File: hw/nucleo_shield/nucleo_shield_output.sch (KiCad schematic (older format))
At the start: 4 parts, among them P2 CONN_01X10, P3 CONN_01X10, U1 74HC595, U2 74HC595

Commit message: Update schematic to add sct and io expander
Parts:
- U1, U2: footprint Housings_DIP:DIP-16__300 -> Housings_DIP:DIP-16_W7.62mm
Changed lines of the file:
@@
 LIBS:memory
 LIBS:xilinx
-LIBS:special
 LIBS:microcontrollers
 LIBS:dsp
@@
 F 0 "U1" H 4650 3250 70  0000 C CNN
 F 1 "74HC595" H 4500 2050 70  0000 C CNN
-F 2 "Housings_DIP:DIP-16__300" H 4500 2650 60  0001 C CNN
+F 2 "Housings_DIP:DIP-16_W7.62mm" H 4500 2650 60  0001 C CNN
 F 3 "" H 4500 2650 60  0000 C CNN
 	1    4500 2650
@@
 $EndComp
 $Comp
-L GND #PWR012
+L GND #PWR021
 U 1 1 5729AB4A
 P 3800 3050
-F 0 "#PWR012" H 3800 2800 50  0001 C CNN
+F 0 "#PWR021" H 3800 2800 50  0001 C CNN
 F 1 "GND" H 3800 2900 50  0000 C CNN
 F 2 "" H 3800 3050 60  0000 C CNN
@@
 $EndComp
 $Comp
-L GND #PWR013
+L GND #PWR022
 U 1 1 5729AB50
 P 3800 4650
-F 0 "#PWR013" H 3800 4400 50  0001 C CNN
+F 0 "#PWR022" H 3800 4400 50  0001 C CNN
 F 1 "GND" H 3800 4500 50  0000 C CNN
 F 2 "" H 3800 4650 60  0000 C CNN
@@
 	7950 4400 8050 4400
 $Comp
-L GND #PWR014
+L GND #PWR023
 U 1 1 5729ABA1
 P 7000 2100
-F 0 "#PWR014" H 7000 1850 50  0001 C CNN
+F 0 "#PWR023" H 7000 1850 50  0001 C CNN
 F 1 "GND" H 7000 1950 50  0000 C CNN
 F 2 "" H 7000 2100 60  0000 C CNN
@@
 	7500 3700 8050 3700
 $Comp
-L +5V #PWR015
+L +5V #PWR024
 U 1 1 5729ABA8
 P 7000 2000
-F 0 "#PWR015" H 7000 1850 50  0001 C CNN
+F 0 "#PWR024" H 7000 1850 50  0001 C CNN
 F 1 "+5V" H 7000 2140 50  0000 C CNN
 F 2 "" H 7000 2000 60  0000 C CNN
@@
 $EndComp
 $Comp
-L +5V #PWR016
+L +5V #PWR025
 U 1 1 5729ABBE
 P 7100 4600
-F 0 "#PWR016" H 7100 4450 50  0001 C CNN
+F 0 "#PWR025" H 7100 4450 50  0001 C CNN
 F 1 "+5V" H 7100 4740 50  0000 C CNN
 F 2 "" H 7100 4600 60  0000 C CNN
@@
 $EndComp
 $Comp
-L GND #PWR017
+L GND #PWR026
 U 1 1 5729ABC4
 P 7100 4500
-F 0 "#PWR017" H 7100 4250 50  0001 C CNN
+F 0 "#PWR026" H 7100 4250 50  0001 C CNN
 F 1 "GND" H 7100 4350 50  0000 C CNN
 F 2 "" H 7100 4500 60  0000 C CNN
@@
 F 0 "U2" H 4650 4850 70  0000 C CNN
 F 1 "74HC595" H 4500 3650 70  0000 C CNN
-F 2 "Housings_DIP:DIP-16__300" H 4500 4250 60  0001 C CNN
+F 2 "Housings_DIP:DIP-16_W7.62mm" H 4500 4250 60  0001 C CNN
 F 3 "" H 4500 4250 60  0000 C CNN
 	1    4500 4250
@@
 $EndComp
 $Comp
-L +5V #PWR018
+L +5V #PWR027
 U 1 1 5729ABD5
 P 4200 1900
-F 0 "#PWR018" H 4200 1750 50  0001 C CNN
+F 0 "#PWR027" H 4200 1750 50  0001 C CNN
 F 1 "+5V" H 4200 2040 50  0000 C CNN
 F 2 "" H 4200 1900 60  0000 C CNN
@@
 $EndComp
 $Comp
-L +5V #PWR019
+L +5V #PWR028
 U 1 1 5729ABDB
 P 5900 3550
-F 0 "#PWR019" H 5900 3400 50  0001 C CNN
+F 0 "#PWR028" H 5900 3400 50  0001 C CNN
 F 1 "+5V" H 5900 3690 50  0000 C CNN
 F 2 "" H 5900 3550 60  0000 C CNN
@@
 	5200 3350 5200 3100
 $Comp
-L +5V #PWR020
+L +5V #PWR029
 U 1 1 5729ABE8
 P 2500 2500
-F 0 "#PWR020" H 2500 2350 50  0001 C CNN
+F 0 "#PWR029" H 2500 2350 50  0001 C CNN
 F 1 "+5V" H 2500 2640 50  0000 C CNN
 F 2 "" H 2500 2500 60  0000 C CNN
@@
 $EndComp
 $Comp
-L +5V #PWR021
+L +5V #PWR030
 U 1 1 5729ABEE
 P 3050 4100
-F 0 "#PWR021" H 3050 3950 50  0001 C CNN
+F 0 "#PWR030" H 3050 3950 50  0001 C CNN
 F 1 "+5V" H 3050 4240 50  0000 C CNN
 F 2 "" H 3050 4100 60  0000 C CNN

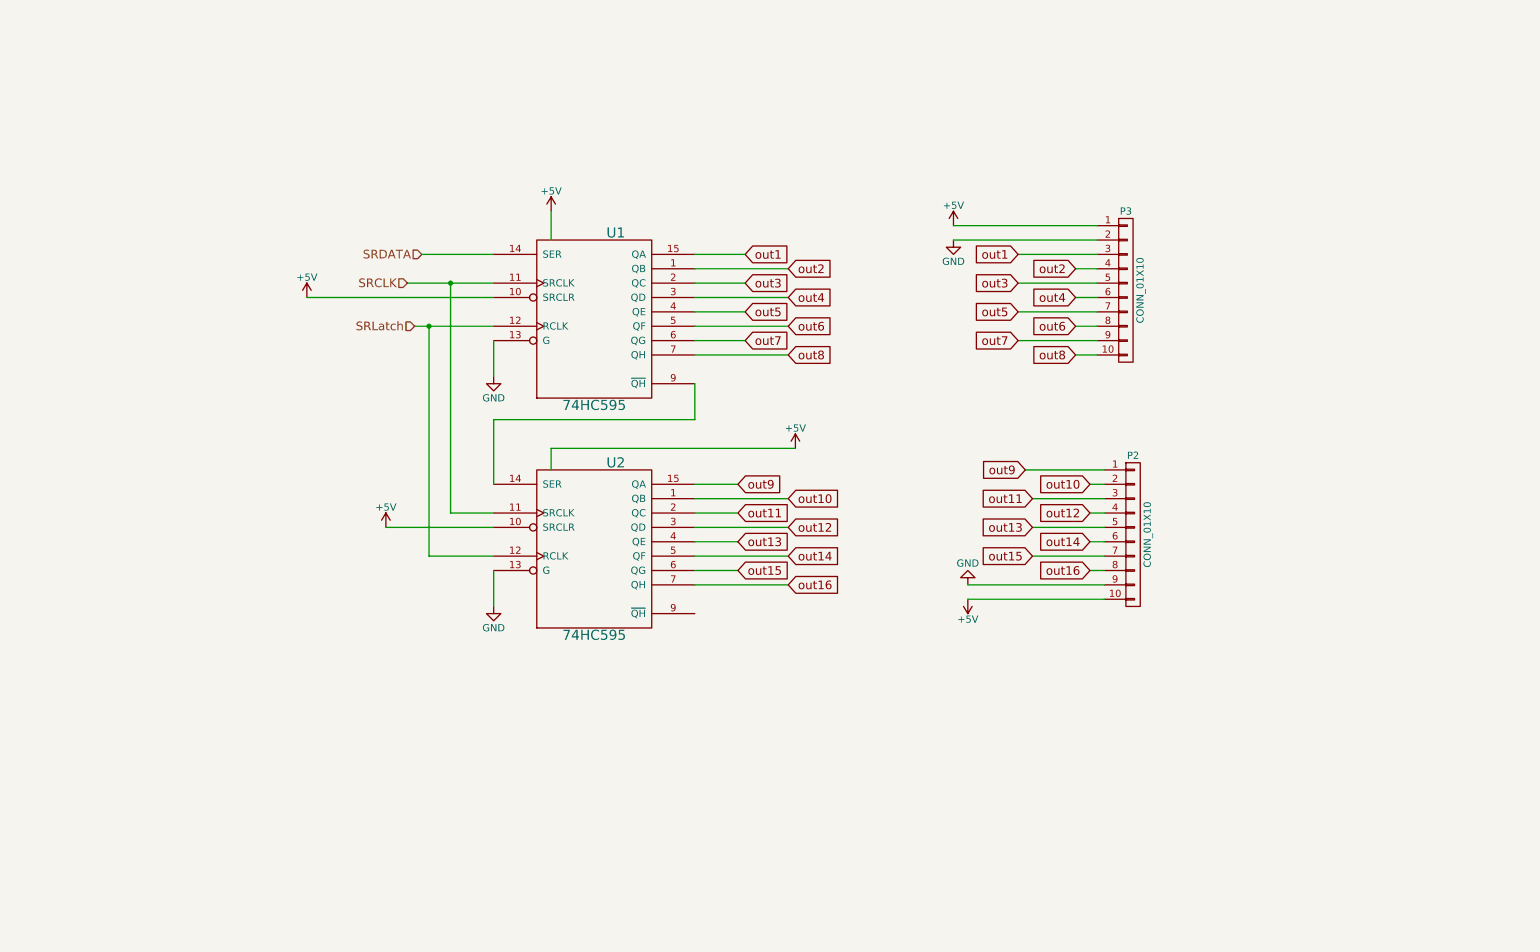
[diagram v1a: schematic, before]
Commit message: Hw: add intermediate header between output and ULN2803
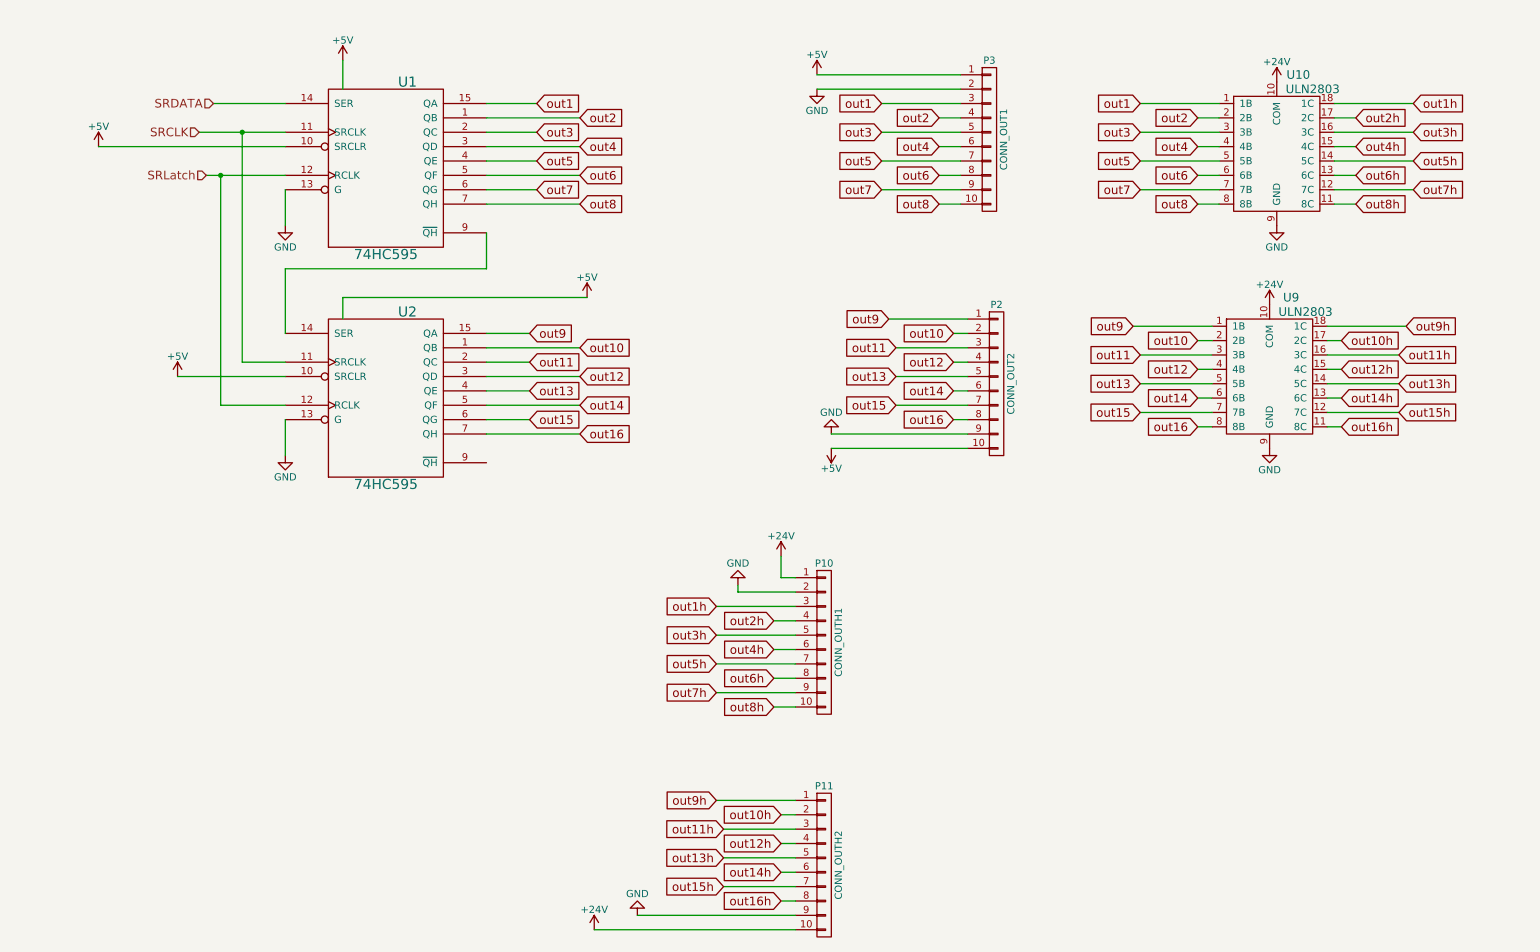
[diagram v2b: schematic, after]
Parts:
- added P10: CONN_OUTH1, w_conn_screw:mors_10p, symbol CONN_01X10
- added P11: CONN_OUTH2, w_conn_screw:mors_10p, symbol CONN_01X10
- added U10, U9: ULN2803, Housings_DIP:DIP-18__300, symbol ULN2803
- P2: value CONN_01X10 -> CONN_OUT2; footprint w_conn_screw:mors_10p -> Pin_Headers:Pin_Header_Straight_1x10
- P3: value CONN_01X10 -> CONN_OUT1; footprint w_conn_screw:mors_10p -> Pin_Headers:Pin_Header_Straight_1x10
- U1, U2: footprint Housings_DIP:DIP-16_W7.62mm -> Housings_DIP:DIP-16__300
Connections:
- net GND: now also P10.2 (P2), P11.9 (P9), U10.9 (GND), U9.9 (GND)
- net out1: now also U10.1 (1B)
- net out10: now also U9.2 (2B)
- net out11: now also U9.3 (3B)
- net out12: now also U9.4 (4B)
- net out13: now also U9.5 (5B)
- net out14: now also U9.6 (6B)
- net out15: now also U9.7 (7B)
- net out16: now also U9.8 (8B)
- net out2: now also U10.2 (2B)
- net out3: now also U10.3 (3B)
- net out4: now also U10.4 (4B)
- net out5: now also U10.5 (5B)
- net out6: now also U10.6 (6B)
- net out7: now also U10.7 (7B)
- net out8: now also U10.8 (8B)
- net out9: now also U9.1 (1B)
- new net +24V: P10.1 (P1), P11.10 (P10), U10.10 (COM), U9.10 (COM)
- new net out10h: P11.2 (P2), U9.17 (2C)
- new net out11h: P11.3 (P3), U9.16 (3C)
- new net out12h: P11.4 (P4), U9.15 (4C)
- new net out13h: P11.5 (P5), U9.14 (5C)
- new net out14h: P11.6 (P6), U9.13 (6C)
- new net out15h: P11.7 (P7), U9.12 (7C)
- new net out16h: P11.8 (P8), U9.11 (8C)
- new net out1h: P10.3 (P3), U10.18 (1C)
- new net out2h: P10.4 (P4), U10.17 (2C)
- new net out3h: P10.5 (P5), U10.16 (3C)
- new net out4h: P10.6 (P6), U10.15 (4C)
- new net out5h: P10.7 (P7), U10.14 (5C)
- new net out6h: P10.8 (P8), U10.13 (6C)
- new net out7h: P10.9 (P9), U10.12 (7C)
- new net out8h: P10.10 (P10), U10.11 (8C)
- new net out9h: P11.1 (P1), U9.18 (1C)
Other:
- moved on the sheet: P2, P3, U1, U2

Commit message: HW: fix a lot of connection and start positionning
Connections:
- net out1: now also U10.8 (8B); no longer U10.1 (1B)
- net out10: now also U9.7 (7B); no longer U9.2 (2B)
- net out10h: now also U9.12 (7C); no longer U9.17 (2C)
- net out11: now also U9.6 (6B); no longer U9.3 (3B)
- net out11h: now also U9.13 (6C); no longer U9.16 (3C)
- net out12: now also U9.5 (5B); no longer U9.4 (4B)
- net out12h: now also U9.14 (5C); no longer U9.15 (4C)
- net out13: now also U9.4 (4B); no longer U9.5 (5B)
- net out13h: now also U9.15 (4C); no longer U9.14 (5C)
- net out14: now also U9.3 (3B); no longer U9.6 (6B)
- net out14h: now also U9.16 (3C); no longer U9.13 (6C)
- net out15: now also U9.2 (2B); no longer U9.7 (7B)
- net out15h: now also U9.17 (2C); no longer U9.12 (7C)
- net out16: now also U9.1 (1B); no longer U9.8 (8B)
- net out16h: now also U9.18 (1C); no longer U9.11 (8C)
- net out1h: now also U10.11 (8C); no longer U10.18 (1C)
- net out2: now also U10.7 (7B); no longer U10.2 (2B)
- net out2h: now also U10.12 (7C); no longer U10.17 (2C)
- net out3: now also U10.6 (6B); no longer U10.3 (3B)
- net out3h: now also U10.13 (6C); no longer U10.16 (3C)
- net out4: now also U10.5 (5B); no longer U10.4 (4B)
- net out4h: now also U10.14 (5C); no longer U10.15 (4C)
- net out5: now also U10.4 (4B); no longer U10.5 (5B)
- net out5h: now also U10.15 (4C); no longer U10.14 (5C)
- net out6: now also U10.3 (3B); no longer U10.6 (6B)
- net out6h: now also U10.16 (3C); no longer U10.13 (6C)
- net out7: now also U10.2 (2B); no longer U10.7 (7B)
- net out7h: now also U10.17 (2C); no longer U10.12 (7C)
- net out8: now also U10.1 (1B); no longer U10.8 (8B)
- net out8h: now also U10.18 (1C); no longer U10.11 (8C)
- net out9: now also U9.8 (8B); no longer U9.1 (1B)
- net out9h: now also U9.11 (8C); no longer U9.18 (1C)
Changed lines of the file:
@@
 LIBS:memory
 LIBS:xilinx
-LIBS:special
 LIBS:microcontrollers
 LIBS:dsp
@@
 $EndComp
 $Comp
-L GND #PWR021
+L GND #PWR020
 U 1 1 5729AB4A
 P 2350 2000
-F 0 "#PWR021" H 2350 1750 50  0001 C CNN
+F 0 "#PWR020" H 2350 1750 50  0001 C CNN
 F 1 "GND" H 2350 1850 50  0000 C CNN
 F 2 "" H 2350 2000 60  0000 C CNN
@@
 $EndComp
 $Comp
-L GND #PWR022
+L GND #PWR021
 U 1 1 5729AB50
 P 2350 3600
-F 0 "#PWR022" H 2350 3350 50  0001 C CNN
+F 0 "#PWR021" H 2350 3350 50  0001 C CNN
 F 1 "GND" H 2350 3450 50  0000 C CNN
 F 2 "" H 2350 3600 60  0000 C CNN
@@
 	7000 3350 7100 3350
 $Comp
-L GND #PWR023
+L GND #PWR022
 U 1 1 5729ABA1
 P 6050 1050
-F 0 "#PWR023" H 6050 800 50  0001 C CNN
+F 0 "#PWR022" H 6050 800 50  0001 C CNN
 F 1 "GND" H 6050 900 50  0000 C CNN
 F 2 "" H 6050 1050 60  0000 C CNN
@@
 	6550 2650 7100 2650
 $Comp
-L +5V #PWR024
+L +5V #PWR023
 U 1 1 5729ABA8
 P 6050 950
-F 0 "#PWR024" H 6050 800 50  0001 C CNN
+F 0 "#PWR023" H 6050 800 50  0001 C CNN
 F 1 "+5V" H 6050 1090 50  0000 C CNN
 F 2 "" H 6050 950 60  0000 C CNN
@@
 $EndComp
 $Comp
-L +5V #PWR025
+L +5V #PWR024
 U 1 1 5729ABBE
 P 6150 3550
-F 0 "#PWR025" H 6150 3400 50  0001 C CNN
+F 0 "#PWR024" H 6150 3400 50  0001 C CNN
 F 1 "+5V" H 6150 3690 50  0000 C CNN
 F 2 "" H 6150 3550 60  0000 C CNN
@@
 $EndComp
 $Comp
-L GND #PWR026
+L GND #PWR025
 U 1 1 5729ABC4
 P 6150 3450
-F 0 "#PWR026" H 6150 3200 50  0001 C CNN
+F 0 "#PWR025" H 6150 3200 50  0001 C CNN
 F 1 "GND" H 6150 3300 50  0000 C CNN
 F 2 "" H 6150 3450 60  0000 C CNN
@@
 $EndComp
 $Comp
-L +5V #PWR027
+L +5V #PWR026
 U 1 1 5729ABD5
 P 2750 850
-F 0 "#PWR027" H 2750 700 50  0001 C CNN
+F 0 "#PWR026" H 2750 700 50  0001 C CNN
 F 1 "+5V" H 2750 990 50  0000 C CNN
 F 2 "" H 2750 850 60  0000 C CNN
@@
 $EndComp
 $Comp
-L +5V #PWR028
+L +5V #PWR027
 U 1 1 5729ABDB
 P 4450 2500
-F 0 "#PWR028" H 4450 2350 50  0001 C CNN
+F 0 "#PWR027" H 4450 2350 50  0001 C CNN
 F 1 "+5V" H 4450 2640 50  0000 C CNN
 F 2 "" H 4450 2500 60  0000 C CNN
@@
 	3750 2300 3750 2050
 $Comp
-L +5V #PWR029
+L +5V #PWR028
 U 1 1 5729ABE8
 P 1050 1450
-F 0 "#PWR029" H 1050 1300 50  0001 C CNN
+F 0 "#PWR028" H 1050 1300 50  0001 C CNN
 F 1 "+5V" H 1050 1590 50  0000 C CNN
 F 2 "" H 1050 1450 60  0000 C CNN
@@
 $EndComp
 $Comp
-L +5V #PWR030
+L +5V #PWR029
 U 1 1 5729ABEE
 P 1600 3050
-F 0 "#PWR030" H 1600 2900 50  0001 C CNN
+F 0 "#PWR029" H 1600 2900 50  0001 C CNN
 F 1 "+5V" H 1600 3190 50  0000 C CNN
 F 2 "" H 1600 3050 60  0000 C CNN
@@
 $EndComp
 $Comp
-L GND #PWR031
+L GND #PWR030
 U 1 1 57307D6B
 P 9250 2000
-F 0 "#PWR031" H 9250 1750 50  0001 C CNN
+F 0 "#PWR030" H 9250 1750 50  0001 C CNN
 F 1 "GND" H 9250 1850 50  0000 C CNN
 F 2 "" H 9250 2000 60  0000 C CNN
@@
 $EndComp
 $Comp
-L GND #PWR032
+L GND #PWR031
 U 1 1 57307D82
 P 9200 3550
-F 0 "#PWR032" H 9200 3300 50  0001 C CNN
+F 0 "#PWR031" H 9200 3300 50  0001 C CNN
 F 1 "GND" H 9200 3400 50  0000 C CNN
 F 2 "" H 9200 3550 60  0000 C CNN
@@
 $EndComp
 $Comp
-L +24V #PWR033
+L +24V #PWR032
 U 1 1 57307DA1
 P 9250 1000
-F 0 "#PWR033" H 9250 850 50  0001 C CNN
+F 0 "#PWR032" H 9250 850 50  0001 C CNN
 F 1 "+24V" H 9250 1140 50  0000 C CNN
 F 2 "" H 9250 1000 60  0000 C CNN
@@
 $EndComp
 $Comp
-L +24V #PWR034
+L +24V #PWR033
 U 1 1 57307DBF
 P 9200 2550
-F 0 "#PWR034" H 9200 2400 50  0001 C CNN
+F 0 "#PWR033" H 9200 2400 50  0001 C CNN
 F 1 "+24V" H 9200 2690 50  0000 C CNN
 F 2 "" H 9200 2550 60  0000 C CNN
@@
 	1    0    0    -1
 $EndComp
+Text GLabel 8700 1850 0    60   Input ~ 0
+out1
+Text GLabel 8300 1750 0    60   Input ~ 0
+out2
+Text GLabel 8700 1650 0    60   Input ~ 0
+out3
+Text GLabel 8300 1550 0    60   Input ~ 0
+out4
+Text GLabel 8700 1450 0    60   Input ~ 0
+out5
+Text GLabel 8300 1350 0    60   Input ~ 0
+out6
+Text GLabel 8700 1250 0    60   Input ~ 0
+out7
 Text GLabel 8300 1150 0    60   Input ~ 0
-out1
-Text GLabel 8700 1250 0    60   Input ~ 0
-out2
-Text GLabel 8300 1350 0    60   Input ~ 0
-out3
-Text GLabel 8700 1450 0    60   Input ~ 0
-out4
-Text GLabel 8300 1550 0    60   Input ~ 0
-out5
-Text GLabel 8700 1650 0    60   Input ~ 0
-out6
-Text GLabel 8300 1750 0    60   Input ~ 0
-out7
-Text GLabel 8700 1850 0    60   Input ~ 0
 out8
 Wire Wire Line
@@
 Wire Wire Line
 	8700 1850 8850 1850
+Text GLabel 8700 3400 0    60   Input ~ 0
+out9
+Text GLabel 8300 3300 0    60   Input ~ 0
+out10
+Text GLabel 8700 3200 0    60   Input ~ 0
+out11
+Text GLabel 8300 3100 0    60   Input ~ 0
+out12
+Text GLabel 8700 3000 0    60   Input ~ 0
+out13
+Text GLabel 8300 2900 0    60   Input ~ 0
+out14
+Text GLabel 8700 2800 0    60   Input ~ 0
+out15
 Text GLabel 8250 2700 0    60   Input ~ 0
-out9
-Text GLabel 8700 2800 0    60   Input ~ 0
-out10
-Text GLabel 8300 2900 0    60   Input ~ 0
-out11
-Text GLabel 8700 3000 0    60   Input ~ 0
-out12
-Text GLabel 8300 3100 0    60   Input ~ 0
-out13
-Text GLabel 8700 3200 0    60   Input ~ 0
-out14
-Text GLabel 8300 3300 0    60   Input ~ 0
-out15
-Text GLabel 8700 3400 0    60   Input ~ 0
 out16
 Wire Wire Line
@@
 	1    0    0    -1
 $EndComp
+Text GLabel 9800 1850 2    60   Input ~ 0
+out1h
+Text GLabel 10200 1750 2    60   Input ~ 0
+out2h
+Text GLabel 9800 1650 2    60   Input ~ 0
+out3h
+Text GLabel 10200 1550 2    60   Input ~ 0
+out4h
+Text GLabel 9800 1450 2    60   Input ~ 0
+out5h
+Text GLabel 10200 1350 2    60   Input ~ 0
+out6h
+Text GLabel 9800 1250 2    60   Input ~ 0
+out7h
 Text GLabel 10200 1150 2    60   Input ~ 0
-out1h
-Text GLabel 9800 1250 2    60   Input ~ 0
-out2h
-Text GLabel 10200 1350 2    60   Input ~ 0
-out3h
-Text GLabel 9800 1450 2    60   Input ~ 0
-out4h
-Text GLabel 10200 1550 2    60   Input ~ 0
-out5h
-Text GLabel 9800 1650 2    60   Input ~ 0
-out6h
-Text GLabel 10200 1750 2    60   Input ~ 0
-out7h
-Text GLabel 9800 1850 2    60   Input ~ 0
 out8h
 Wire Wire Line
@@
 Wire Wire Line
 	9800 1850 9650 1850
+Text GLabel 9700 3400 2    60   Input ~ 0
+out9h
+Text GLabel 10100 3300 2    60   Input ~ 0
+out10h
+Text GLabel 9700 3200 2    60   Input ~ 0
+out11h
+Text GLabel 10100 3100 2    60   Input ~ 0
+out12h
+Text GLabel 9700 3000 2    60   Input ~ 0
+out13h
+Text GLabel 10100 2900 2    60   Input ~ 0
+out14h
+Text GLabel 9700 2800 2    60   Input ~ 0
+out15h
 Text GLabel 10150 2700 2    60   Input ~ 0
-out9h
-Text GLabel 9700 2800 2    60   Input ~ 0
-out10h
-Text GLabel 10100 2900 2    60   Input ~ 0
-out11h
-Text GLabel 9700 3000 2    60   Input ~ 0
-out12h
-Text GLabel 10100 3100 2    60   Input ~ 0
-out13h
-Text GLabel 9700 3200 2    60   Input ~ 0
-out14h
-Text GLabel 10100 3300 2    60   Input ~ 0
-out15h
-Text GLabel 9700 3400 2    60   Input ~ 0
 out16h
 Wire Wire Line
@@
 	5750 5350 5900 5350
 $Comp
-L GND #PWR035
+L GND #PWR034
 U 1 1 573085F0
 P 5500 4500
-F 0 "#PWR035" H 5500 4250 50  0001 C CNN
+F 0 "#PWR034" H 5500 4250 50  0001 C CNN
 F 1 "GND" H 5500 4350 50  0000 C CNN
 F 2 "" H 5500 4500 60  0000 C CNN
@@
 $EndComp
 $Comp
-L GND #PWR036
+L GND #PWR035
 U 1 1 5730860B
 P 4800 6800
-F 0 "#PWR036" H 4800 6550 50  0001 C CNN
+F 0 "#PWR035" H 4800 6550 50  0001 C CNN
 F 1 "GND" H 4800 6650 50  0000 C CNN
 F 2 "" H 4800 6800 60  0000 C CNN
@@
 	5900 6800 4800 6800
 $Comp
-L +24V #PWR037
+L +24V #PWR036
 U 1 1 573087B8
 P 5800 4300
-F 0 "#PWR037" H 5800 4150 50  0001 C CNN
+F 0 "#PWR036" H 5800 4150 50  0001 C CNN
 F 1 "+24V" H 5800 4440 50  0000 C CNN
 F 2 "" H 5800 4300 60  0000 C CNN
@@
 	5800 4450 5900 4450
 $Comp
-L +24V #PWR038
+L +24V #PWR037
 U 1 1 5730884E
 P 4500 6900
-F 0 "#PWR038" H 4500 6750 50  0001 C CNN
+F 0 "#PWR037" H 4500 6750 50  0001 C CNN
 F 1 "+24V" H 4500 7040 50  0000 C CNN
 F 2 "" H 4500 6900 60  0000 C CNN
